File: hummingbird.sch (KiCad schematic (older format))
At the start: 1 part

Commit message: start adding wires
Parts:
- added C?: 1uF, symbol Device:C_Small
- U?: symbol MCU_Microchip_SAMD:ATSAMD21G18A-AUT -> symbols:ATSAMD21G18A-AUT
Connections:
- net labels added: +3V3, GND, RESET, SWCLK, SWDIO
- wire segments 0 -> 17
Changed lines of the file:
@@
 EESchema Schematic File Version 4
+LIBS:hummingbird-cache
 EELAYER 29 0
 EELAYER END
@@
 $EndDescr
 $Comp
-L MCU_Microchip_SAMD:ATSAMD21G18A-AUT U?
+L symbols:ATSAMD21G18A-AUT U?
 U 1 1 5CEC88D0
 P 2400 5150
 F 0 "U?" H 2400 3161 50  0000 C CNN
-F 1 "ATSAMD21G18A-AUT" H 2400 3070 50  0000 C CNN
+F 1 "ATSAMD21G18A-AUT" H 3150 3250 50  0000 C CNN
 F 2 "Package_QFP:TQFP-48_7x7mm_P0.5mm" H 1450 3400 50  0001 C CNN
 F 3 "http://ww1.microchip.com/downloads/en/DeviceDoc/SAMD21-Family-DataSheet-DS40001882D.pdf" H 2400 6150 50  0001 C CNN
@@
 	1    0    0    -1
 $EndComp
+Wire Wire Line
+	2600 3250 2600 2700
+Wire Wire Line
+	2600 2700 3000 2700
+Wire Wire Line
+	3000 2700 3000 2800
+$Comp
+L Device:C_Small C?
+U 1 1 5CF3E2FE
+P 3000 2900
+F 0 "C?" H 3092 2946 50  0000 L CNN
+F 1 "1uF" H 3092 2855 50  0000 L CNN
+F 2 "" H 3000 2900 50  0001 C CNN
+F 3 "~" H 3000 2900 50  0001 C CNN
+	1    3000 2900
+	1    0    0    -1
+$EndComp
+Wire Wire Line
+	3000 3000 3000 3200
+$Comp
+L power:GND #PWR?
+U 1 1 5CF3EB72
+P 3000 3200
+F 0 "#PWR?" H 3000 2950 50  0001 C CNN
+F 1 "GND" H 3005 3027 50  0000 C CNN
+F 2 "" H 3000 3200 50  0001 C CNN
+F 3 "" H 3000 3200 50  0001 C CNN
+	1    3000 3200
+	1    0    0    -1
+$EndComp
+Wire Wire Line
+	2300 7050 2300 7300
+$Comp
+L power:GND #PWR?
+U 1 1 5CF3F526
+P 2300 7350
+F 0 "#PWR?" H 2300 7100 50  0001 C CNN
+F 1 "GND" H 2305 7177 50  0000 C CNN
+F 2 "" H 2300 7350 50  0001 C CNN
+F 3 "" H 2300 7350 50  0001 C CNN
+	1    2300 7350
+	1    0    0    -1
+$EndComp
+Wire Wire Line
+	2500 7050 2500 7300
+Wire Wire Line
+	2300 7300 2500 7300
+Connection ~ 2300 7300
+Wire Wire Line
+	2300 7300 2300 7350
+Wire Wire Line
+	1400 6650 1100 6650
+Text Label 1100 6650 0    50   ~ 0
+RESET
+Wire Wire Line
+	1400 6350 1100 6350
+Wire Wire Line
+	1400 6450 1100 6450
+Text Label 1100 6350 0    50   ~ 0
+SWCLK
+Text Label 1100 6450 0    50   ~ 0
+SWDIO
+Wire Wire Line
+	2500 3250 2500 2700
+$Comp
+L power:+3V3 #PWR?
+U 1 1 5CF40C99
+P 2500 2450
+F 0 "#PWR?" H 2500 2300 50  0001 C CNN
+F 1 "+3V3" H 2515 2623 50  0000 C CNN
+F 2 "" H 2500 2450 50  0001 C CNN
+F 3 "" H 2500 2450 50  0001 C CNN
+	1    2500 2450
+	1    0    0    -1
+$EndComp
+Wire Wire Line
+	2300 3250 2300 2700
+Wire Wire Line
+	2300 2700 2500 2700
+Connection ~ 2500 2700
+Wire Wire Line
+	2500 2700 2500 2450
+Wire Wire Line
+	2200 3250 2200 2700
+Wire Wire Line
+	2200 2700 2300 2700
+Connection ~ 2300 2700
 $EndSCHEMATC

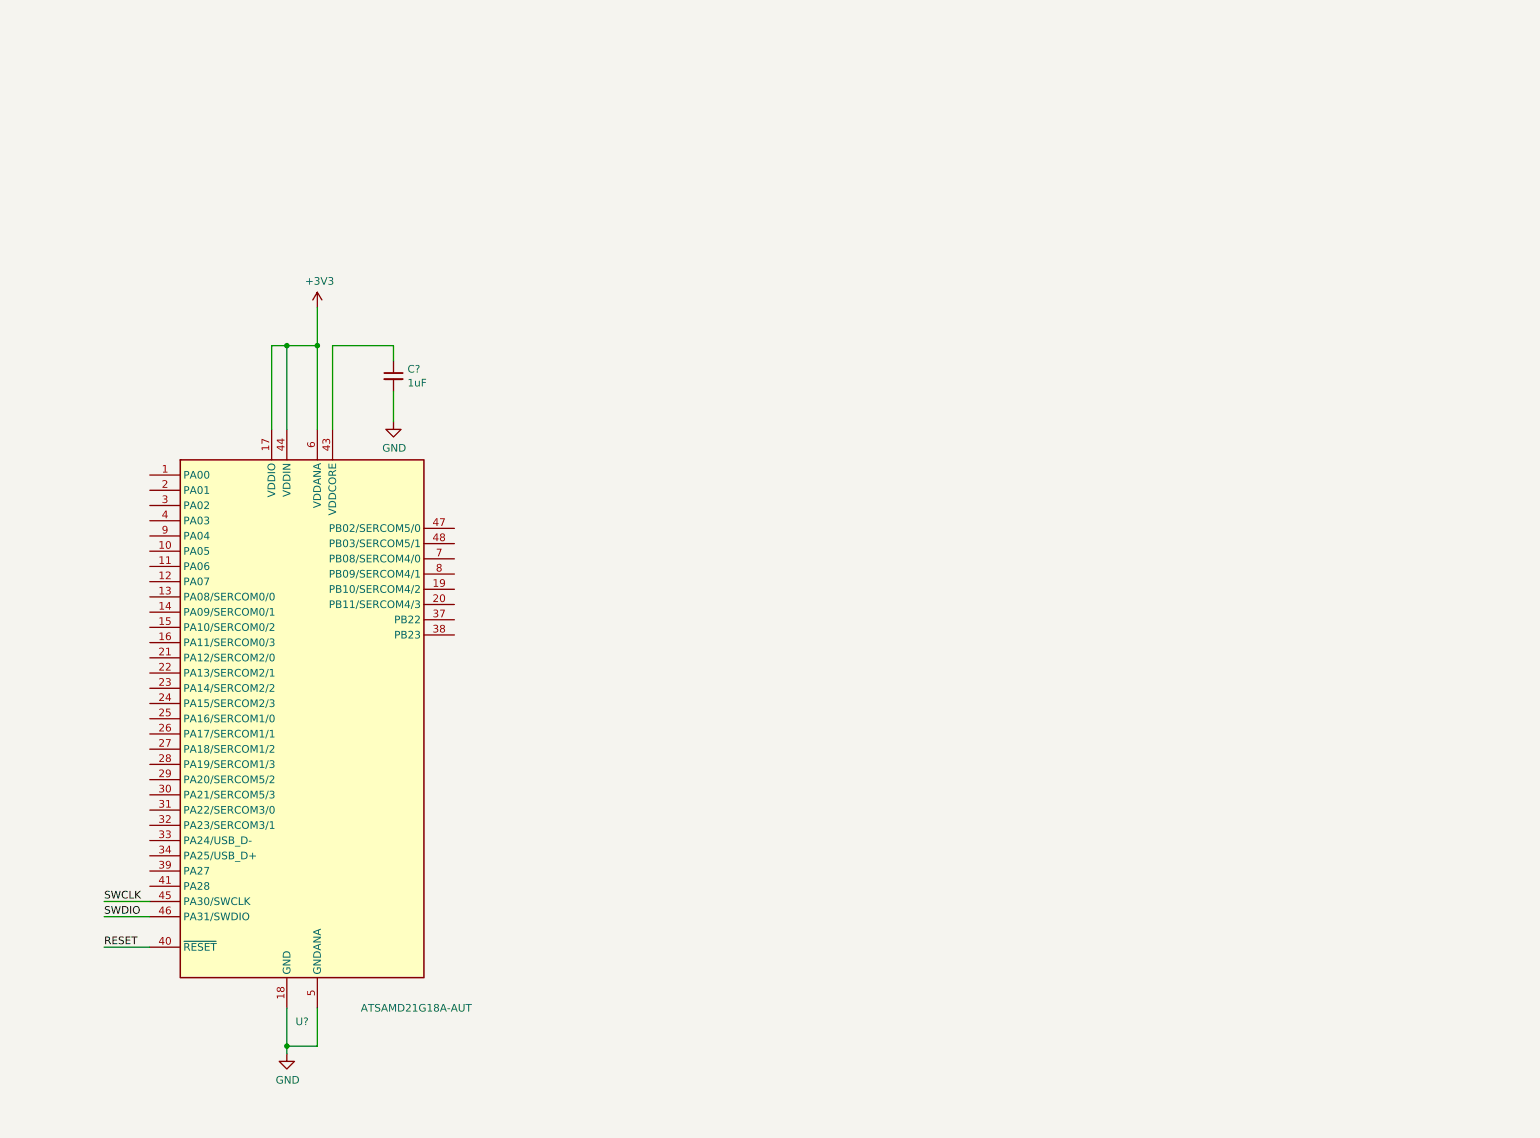
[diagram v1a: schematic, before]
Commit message: add power, charging and bmp388
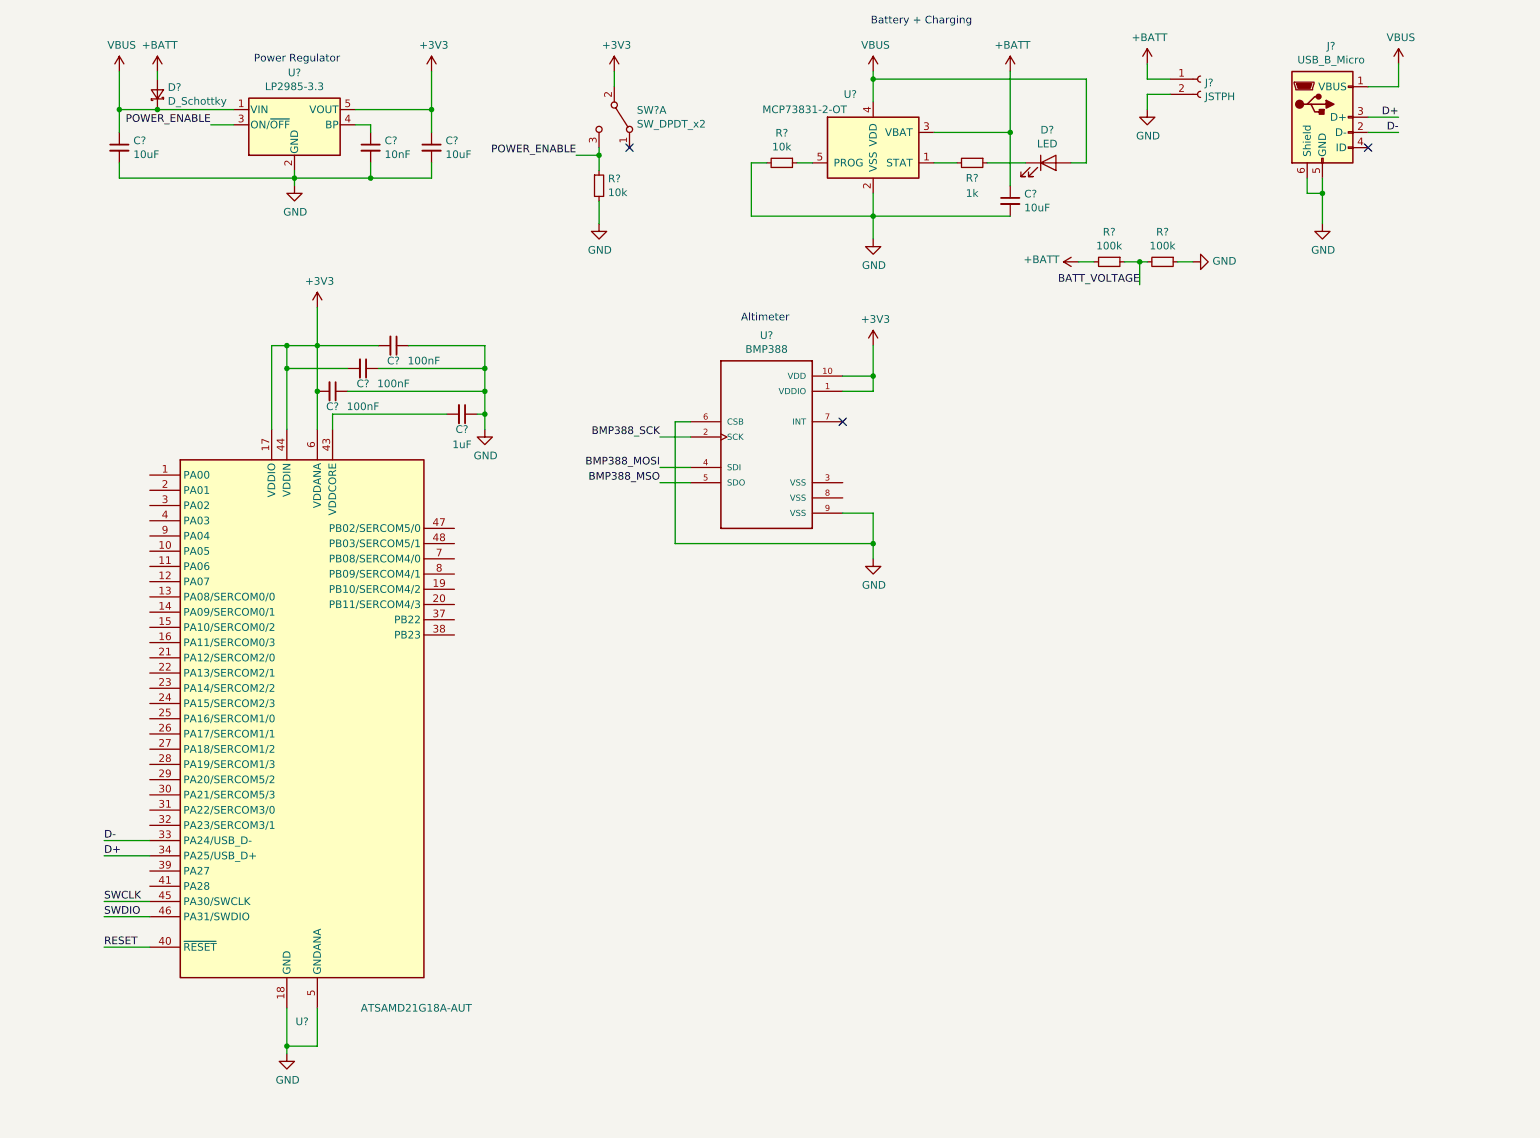
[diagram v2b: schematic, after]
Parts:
- added C? (x3): 100nF, symbol Device:C_Small
- added C? (x3): 10uF, symbol Device:C_Small
- added C?: 10nF, symbol Device:C_Small
- added D?: D_Schottky, symbol Device:D_Schottky_Small
- added D?: LED, symbol Device:LED
- added J?: JSTPH, symbol Connector:Conn_01x02_Female
- added J?: USB_B_Micro, symbol Connector:USB_B_Micro
- added R? (x2): 10k, symbol Device:R_Small
- added R?: 1k, symbol Device:R_Small
- added R? (x2): 100k, symbol Device:R_Small
- added SW?: SW_DPDT_x2, symbol Switch:SW_DPDT_x2
- added U?: LP2985-3.3, Package_TO_SOT_SMD:SOT-23-5, symbol symbols:LP2985-3.3
- added U?: MCP73831-2-OT, Package_TO_SOT_SMD:SOT-23-5, symbol Battery_Management:MCP73831-2-OT
- added U?: BMP388, PQFN50P200X200X80-10N, symbol symbols:BMP388
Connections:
- net +3V3: now also C?.1, C?.2, C?.2, C?.2, SW?.2 (B), U?.1 (VDDIO), U?.10 (VDD), U?.5 (VOUT)
- net GND: now also C?.1, C?.1, C?.1, C?.1, C?.2, C?.2, C?.2, C?.2, J?.2 (Pin_2), J?.5 (GND), J?.6 (Shield), R?.1, R?.2, R?.2, U?.2 (GND), U?.2 (VSS), U?.6 (CSB), U?.9 (VSS); no longer C?.2
- net D-: now reaches U?.33 (PA24/USB_D-)
- net D-: now also J?.2 (D-)
- net D+: now reaches U?.34 (PA25/USB_D+)
- net D+: now also J?.3 (D+)
- net at U?.43 (VDDCORE): now also C?.2; no longer C?.1
- new net: C?.1, U?.4 (BP)
- new net: R?.2, U?.1 (STAT)
- new net: R?.1, U?.5 (PROG)
- new net: D?.1 (K), R?.1
- new net +BATT: C?.1, D?.2 (A), J?.1 (Pin_1), R?.2, U?.3 (VBAT)
- new net BATT_VOLTAGE: R?.1, R?.2
- new net BMP388_MOSI: U?.4 (SDI)
- new net BMP388_MSO: U?.5 (SDO)
- new net BMP388_SCK: U?.2 (SCK)
- new net POWER_ENABLE: R?.1, SW?.3 (C), U?.3 (ON/~OFF~)
- new net VBUS: C?.1, D?.1 (K), D?.2 (A), J?.1 (VBUS), U?.1 (VIN), U?.4 (VDD)
- no-connect marks 0 -> 3
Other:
- note added: "Altimeter"
- note added: "Battery + Charging"
- note added: "Power Regulator\n"
- moved on the sheet: C?

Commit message: spi flash, lora and microsd added
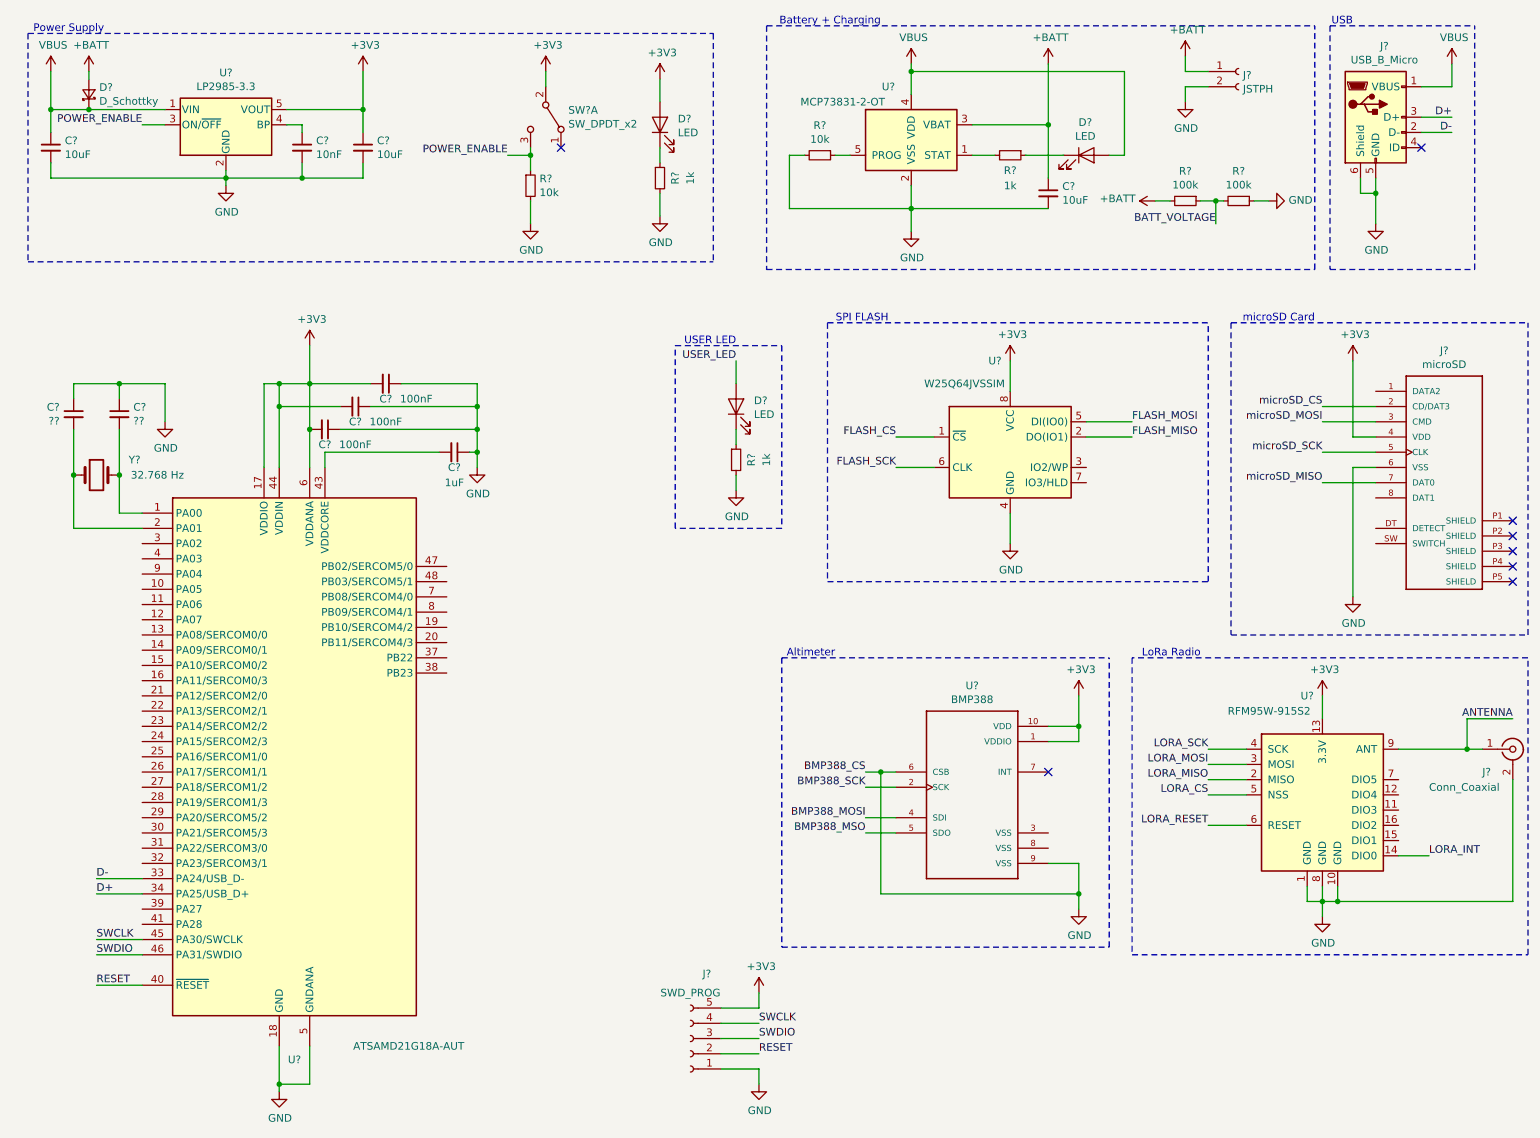
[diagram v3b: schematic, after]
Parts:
- added C? (x2): ??, symbol Device:C_Small
- added D? (x2): LED, symbol Device:LED
- added J?: microSD, MOLEX_503182-1852, symbol symbols:microSD
- added J?: Conn_Coaxial, symbol Connector:Conn_Coaxial
- added J?: SWD_PROG, symbol Connector:Conn_01x05_Female
- added R? (x2): 1k, symbol Device:R_Small
- added U?: W25Q64JVSSIM, Package_SO:SOIC-8_5.23x5.23mm_P1.27mm, symbol symbols:W25Q64JVSSIM
- added U?: RFM95W-915S2, symbol RF_Module:RFM95W-915S2
- added Y?: 32.768 Hz, symbol Device:Crystal
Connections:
- net +3V3: now also D?.2 (A), J?.4 (VDD), J?.5 (Pin_5), U?.13 (3.3V), U?.8 (VCC)
- net GND: now also C?.1, C?.1, J?.1 (Pin_1), J?.2 (Ext), J?.6 (VSS), R?.2, R?.2, U?.1 (GND), U?.10 (GND), U?.4 (GND), U?.8 (GND)
- net RESET: now also J?.2 (Pin_2)
- net SWCLK: now also J?.4 (Pin_4)
- net SWDIO: now also J?.3 (Pin_3)
- net at U?.1 (PA00): now also C?.2, Y?.2
- net at U?.2 (PA01): now also C?.2, Y?.1
- new net: D?.1 (K), R?.1 (x2)
- new net ANTENNA: J?.1 (In), U?.9 (ANT)
- new net FLASH_CS: U?.1 (~CS)
- new net FLASH_MISO: U?.2 (DO(IO1))
- new net FLASH_MOSI: U?.5 (DI(IO0))
- new net FLASH_SCK: U?.6 (CLK)
- new net LORA_CS: U?.5 (NSS)
- new net LORA_INT: U?.14 (DIO0)
- new net LORA_MISO: U?.2 (MISO)
- new net LORA_MOSI: U?.3 (MOSI)
- new net LORA_RESET: U?.6 (RESET)
- new net LORA_SCK: U?.4 (SCK)
- new net USER_LED: D?.2 (A)
- new net microSD_CS: J?.2 (CD/DAT3)
- new net microSD_MISO: J?.7 (DAT0)
- new net microSD_MOSI: J?.3 (CMD)
- new net microSD_SCK: J?.5 (CLK)
- no-connect marks 3 -> 8
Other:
- note added: "LoRa Radio"
- note added: "Power Supply"
- note added: "SPI FLASH"
- note added: "USB"
- note added: "USER LED"
- note added: "microSD Card"
- note removed: "Power Regulator\n"
- moved on the sheet: C?, D?, J?, R?, SW?A, U?
